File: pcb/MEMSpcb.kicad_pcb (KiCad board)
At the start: 4 copper layers, 24.6 x 14.7 mm, 4 parts, among them J2 Conn_02x04_Odd_Even

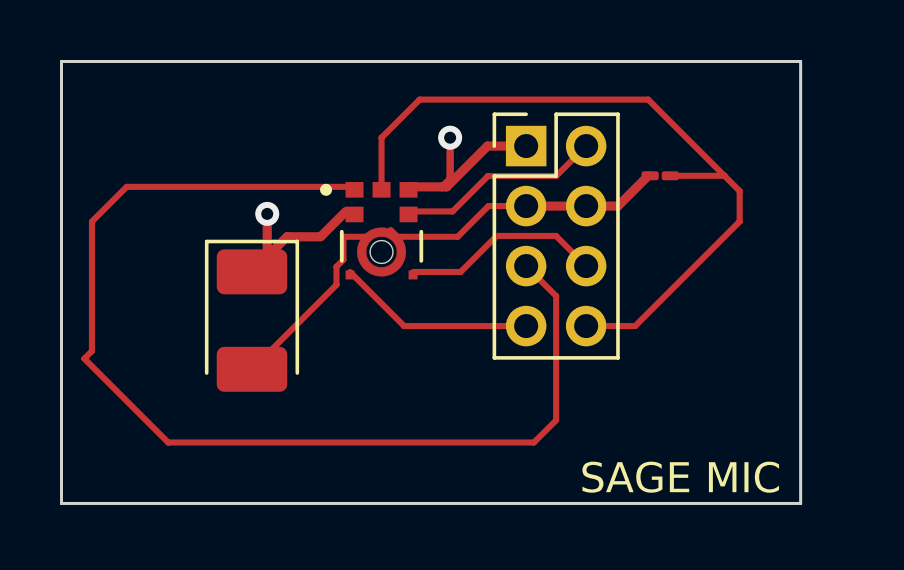
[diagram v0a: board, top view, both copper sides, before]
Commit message: fixed routing sizes, pad error, and resistor error
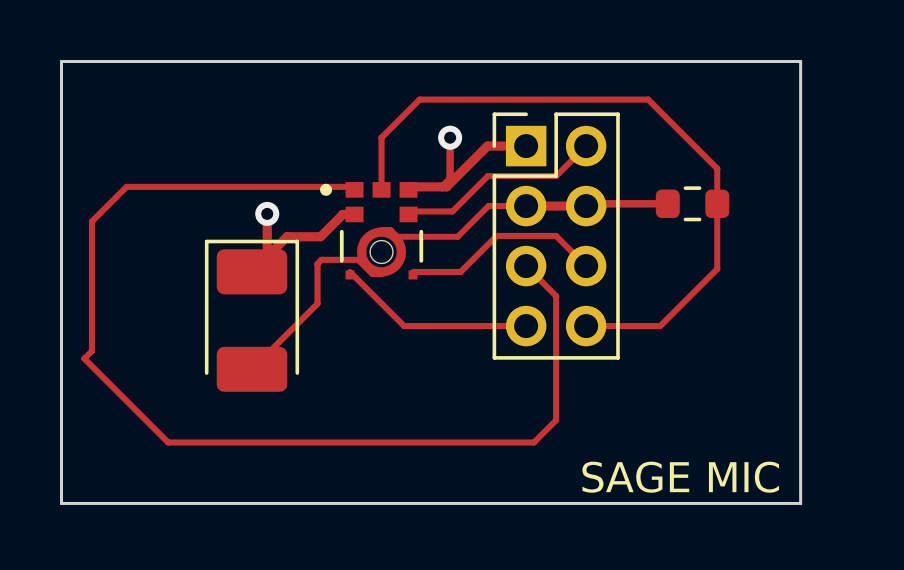
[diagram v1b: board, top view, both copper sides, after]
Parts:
- R1: footprint Resistor_SMD:R_01005_0402Metric_Pad0.57x0.30mm_HandSolder -> Resistor_SMD:R_0603_1608Metric
- moved R1 1.43 mm to (130.0, 84.5)
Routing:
- net /SD: track 24.5 -> 22.8 mm
- net GND: track 15.9 -> 16.9 mm
